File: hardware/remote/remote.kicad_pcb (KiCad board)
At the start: 2 copper layers, 0 parts

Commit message: hardware(remote): first-pass PCB layout (placement + netlist + outline)
Bootstraps the remote board PCB from the captured schematic.

- gen_remote_pcb.py: kiutils-based PCB generator. Loads real KiCad footprints,
  places every part in functional groups (charge/power on the left, DevKit on
  the right, three button stacks along the bottom), assigns the full schematic
  netlist to the pads, and draws the Edge.Cuts outline (78x60mm). Includes a
  pad-bbox overlap self-check (no GUI DRC here). Traces + GND pour are the next
  pass. Netlist is taken from a freshly generated kiutils-native schematic, not
  the committed file, because KiCad re-saved the schematic into a newer format
  that kiutils under-parses.

- Custom footprint IoT_AC_Dimmer:ESP32-DevKitC-30 (30-pin DevKit V1, two 1x15
  rows at 0.9in). Registered via project fp-lib-tables. Schematic footprint
  field updated to reference it (was a non-existent placeholder).

- gen_remote.py: REMOTE_SCH_OUT env override so tooling can emit a scratch
  schematic without touching the committed one.

Verified: 17 footprints, 8 nets, 48 netted pads, no overlaps, in-outline.

NOTE (first pass to verify in KiCad): the DevKit footprint row spacing (0.9in)
and the TP4056-module pad mapping should be checked against the physical parts
before fab; routing and the GND pour are still to do.
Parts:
- added BT1: BT1, JST_PH_S2B-PH-SM4-TB_1x02-1MP_P2.00mm_Horizontal, F.Cu at (12.0, 8.00)
- added C2: C2, C_0805_2012Metric, F.Cu at (23.0, 20.0)
- added C3: C3, C_0805_2012Metric, F.Cu at (33.0, 20.0)
- added C4: C4, C_1206_3216Metric, F.Cu at (30.0, 30.0)
- added C5: C5, C_0805_2012Metric, F.Cu at (37.0, 30.0)
- added C6: C6, C_0805_2012Metric, F.Cu at (11.0, 47.0)
- added C7: C7, C_0805_2012Metric, F.Cu at (25.0, 47.0)
- added C8: C8, C_0805_2012Metric, F.Cu at (39.0, 47.0)
- added R4: R4, R_0805_2012Metric, F.Cu at (11.0, 42.0)
- added R5: R5, R_0805_2012Metric, F.Cu at (25.0, 42.0)
- added R6: R6, R_0805_2012Metric, F.Cu at (39.0, 42.0)
- added SW1: SW1, SW_PUSH_6mm, F.Cu at (11.0, 53.0)
- added SW2: SW2, SW_PUSH_6mm, F.Cu at (25.0, 53.0)
- added SW3: SW3, SW_PUSH_6mm, F.Cu at (39.0, 53.0)
- added U1: U1, PinHeader_1x06_P2.54mm_Vertical, F.Cu at (10.0, 18.0)
- added U2: U2, SOT-23-5, F.Cu at (28.0, 12.0)
- added U3: U3, ESP32-DevKitC-30, F.Cu at (56.0, 30.0)
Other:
- board outline added: 78 x 60 mm
- rule pad_to_mask_clearance: 0 -> 0.0

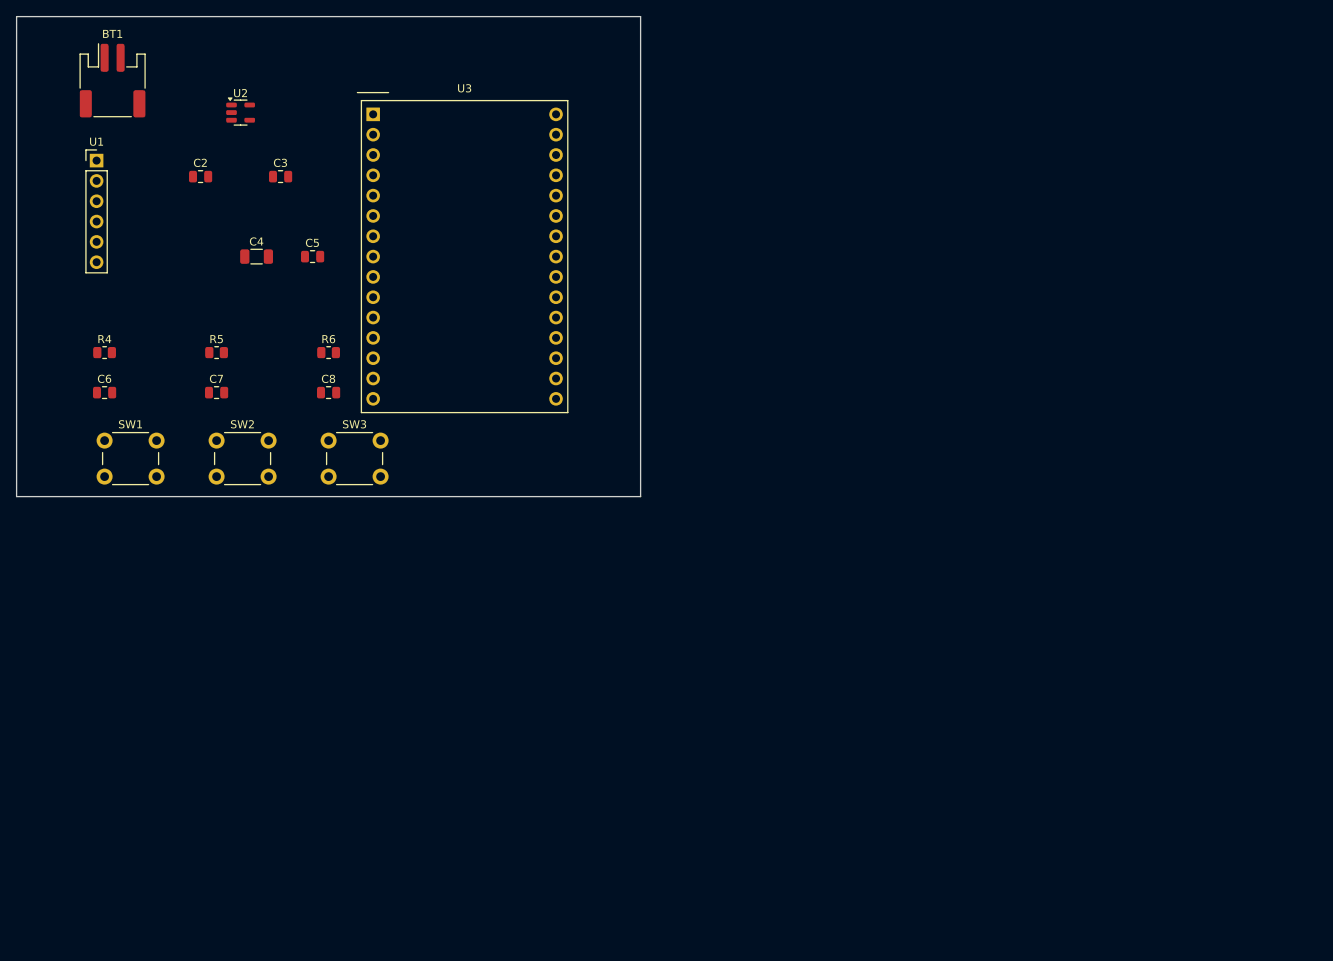
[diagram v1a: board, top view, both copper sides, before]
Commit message: pcb: Update PCB design and Child item name
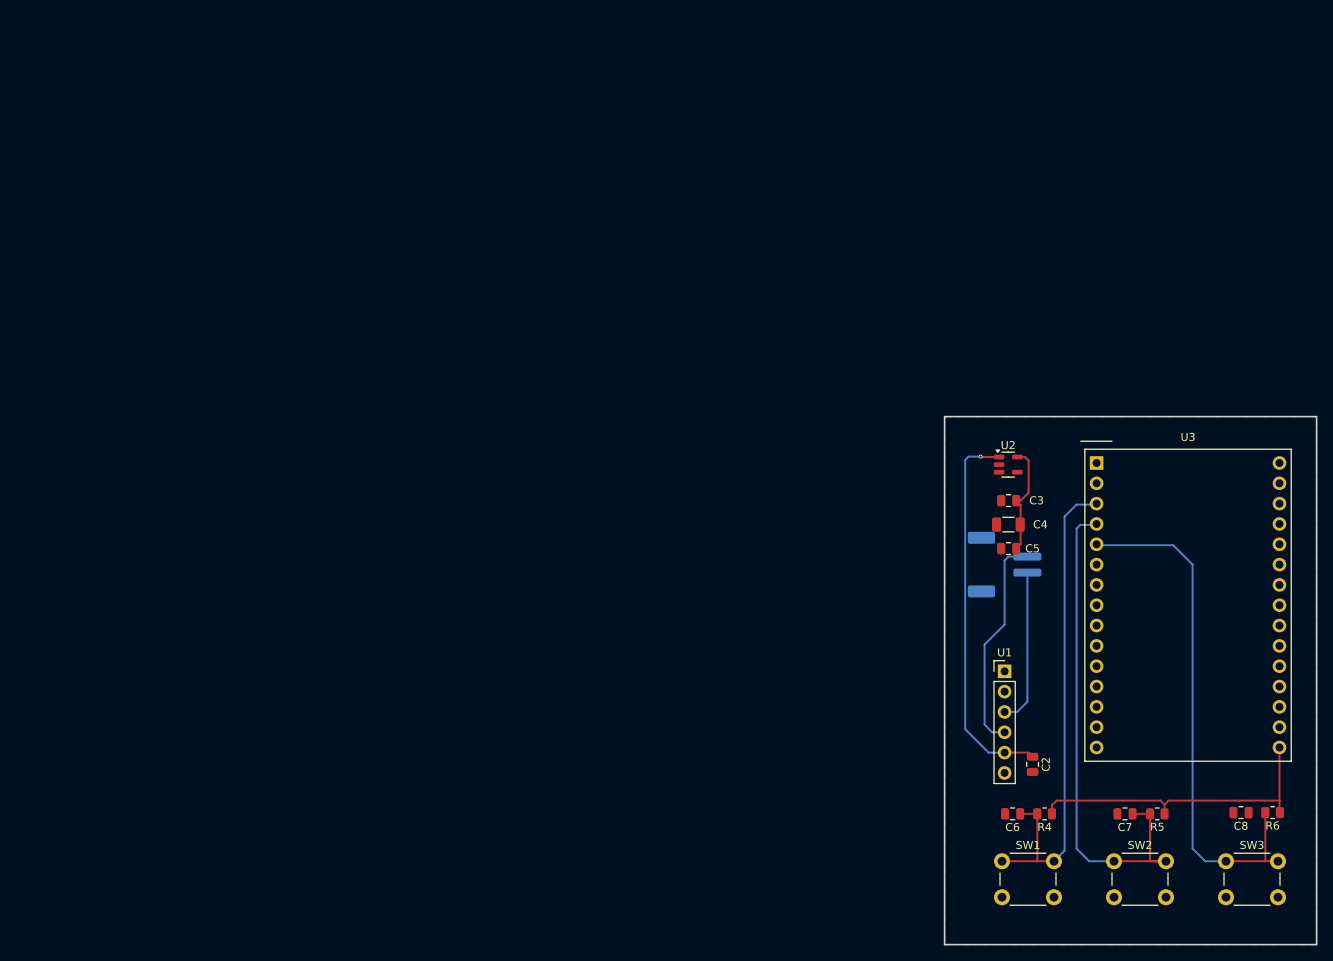
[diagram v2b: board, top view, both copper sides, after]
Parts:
- BT1: value BT1 -> LiPo_500mAh; moved to B.Cu
- C2: value C2 -> 1uF
- C3: value C3 -> 1uF
- C4: value C4 -> 10uF
- C5: value C5 -> 100nF
- C6: value C6 -> 100nF
- C7: value C7 -> 100nF
- C8: value C8 -> 100nF
- R4: value R4 -> 100k
- R5: value R5 -> 100k
- R6: value R6 -> 100k
- SW1: value SW1 -> UP
- SW2: value SW2 -> DOWN
- SW3: value SW3 -> ON/OFF
- U1: value U1 -> TP4056-Module
- U2: value U2 -> ME6211C33M5G
- U3: value U3 -> ESP32-DevKitC-30; footprint ESP32-DevKitC-30 -> IoT_AC_Dimmer:ESP32-DevKitC-30
- moved R6 131.3 mm to (157.0, 99.5), turned to 180 degrees
- moved R5 131.0 mm to (142.6, 99.7), turned to 180 degrees
- moved R4 130.9 mm to (128.5, 99.7), turned to 180 degrees
- moved U1 130.2 mm to (123.5, 81.8)
- moved C2 127.3 mm to (127.0, 93.5), turned to -90 degrees
- moved BT1 126.9 mm to (123.5, 68.5), turned to 90 degrees
- moved C8 125.6 mm to (153.1, 99.5), turned to 180 degrees
- moved C7 125.2 mm to (138.6, 99.7), turned to 180 degrees
- moved C6 125.1 mm to (124.5, 99.7), turned to 180 degrees
- moved SW2 123.9 mm to (137.2, 105.6)
- moved SW3 123.9 mm to (151.2, 105.6)
- moved SW1 123.9 mm to (123.2, 105.6)
- moved U2 105.6 mm to (124.0, 56.0)
- moved U3 100.4 mm to (146.4, 73.6)
- moved C4 99.8 mm to (124.0, 63.5), turned to 180 degrees
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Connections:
- net BATT_N renamed /BATT_N
- net BTN_DOWN renamed /BTN_DOWN
- net BTN_ONOFF renamed /BTN_ONOFF
- net BTN_UP renamed /BTN_UP
- net VBAT renamed /VBAT
- net VSYS renamed /VSYS
- U1 pad 1: (no net) -> unconnected-(U1-IN+-Pad1)
- U1 pad 2: (no net) -> unconnected-(U1-IN--Pad2)
- U2 pad 4: (no net) -> unconnected-(U2-NC-Pad4)
- U3 pad 1: (no net) -> unconnected-(U3-EN-Pad1)
- U3 pad 10: (no net) -> unconnected-(U3-IO27-Pad10)
- U3 pad 11: (no net) -> unconnected-(U3-IO14-Pad11)
- U3 pad 12: (no net) -> unconnected-(U3-IO12-Pad12)
- U3 pad 14: (no net) -> unconnected-(U3-IO13-Pad14)
- U3 pad 15: (no net) -> unconnected-(U3-VIN-Pad15)
- U3 pad 17: (no net) -> unconnected-(U3-IO23-Pad17)
- U3 pad 18: (no net) -> unconnected-(U3-IO22-Pad18)
- U3 pad 19: (no net) -> unconnected-(U3-IO1/TX0-Pad19)
- U3 pad 2: (no net) -> unconnected-(U3-IO36/VP-Pad2)
- U3 pad 20: (no net) -> unconnected-(U3-IO3/RX0-Pad20)
- U3 pad 21: (no net) -> unconnected-(U3-IO21-Pad21)
- U3 pad 22: (no net) -> unconnected-(U3-IO19-Pad22)
- U3 pad 23: (no net) -> unconnected-(U3-IO18-Pad23)
- U3 pad 24: (no net) -> unconnected-(U3-IO5-Pad24)
- U3 pad 25: (no net) -> unconnected-(U3-IO17-Pad25)
- U3 pad 26: (no net) -> unconnected-(U3-IO16-Pad26)
- U3 pad 27: (no net) -> unconnected-(U3-IO4-Pad27)
- U3 pad 28: (no net) -> unconnected-(U3-IO2-Pad28)
- U3 pad 29: (no net) -> unconnected-(U3-IO15-Pad29)
- U3 pad 6: (no net) -> unconnected-(U3-IO32-Pad6)
- U3 pad 7: (no net) -> unconnected-(U3-IO33-Pad7)
- U3 pad 8: (no net) -> unconnected-(U3-IO25-Pad8)
- U3 pad 9: (no net) -> unconnected-(U3-IO26-Pad9)
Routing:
- net /BTN_ONOFF: track 0.00 -> 65.9 mm
- net /BTN_DOWN: track 0.00 -> 64.6 mm
- net /BTN_UP: track 0.00 -> 62.8 mm
- net +3V3: track 0.00 -> 53.4 mm
- net /VSYS: track 0.00 -> 47.9 mm, vias 0 -> 1
- net /BATT_N: track 0.00 -> 27.5 mm
- net /VBAT: track 0.00 -> 19.5 mm
- added copper zone on F.Cu, net GND
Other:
- board size 78 x 60 mm -> 46.5 x 66 mm
- rule pad_to_mask_clearance: 0.0 -> 0
